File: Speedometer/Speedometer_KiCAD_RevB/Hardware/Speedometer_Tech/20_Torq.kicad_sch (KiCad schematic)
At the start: 20 parts, among them U204 WS2812B-4020_2, U205 WS2812B-4020_2, U206 WS2812B-4020_2, U207 WS2812B-4020_2, U208 WS2812B-4020_2, U209 WS2812B-4020_2, U210 WS2812B-4020_2, U211 WS2812B-4020_2, U212 WS2812B-4020_2, U213 WS2812B-4020_2, U214 WS2812B-4020_2, U215 WS2812B-4020_2, U216 WS2812B-4020_2, U217 WS2812B-4020_2, U218 WS2812B-4020_2, U219 WS2812B-4020_2, U220 WS2812B-4020_2, U221 WS2812B-4020_2, U222 WS2812B-4020_2, U223 WS2812B-4020_2

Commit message: updated troq display with new neopixel
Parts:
- added U224, U225, U226, U227, U228, U229, U230, U231, U232, U233, U234, U235, U236, U237, U238, U239, U240, U241: WS2812B-4020_2, LED_SMD:LED_WS2812B-2020_PLCC4_2.0x2.0mm, symbol LED:WS2812B-2020
- U204, U205, U206, U207, U208, U209, U210, U211: footprint LED_WS2812B-4020 -> LED_SMD:LED_WS2812B-2020_PLCC4_2.0x2.0mm; symbol Speedometer_Tech-altium-import:Designator_0_WS2812B-4020_2 -> LED:WS2812B-2020
- U212, U213, U214, U215, U216, U217, U218, U219, U220, U221, U222, U223: footprint LED_WS2812B-4020 -> LED_SMD:LED_WS2812B-2020_PLCC4_2.0x2.0mm; symbol Speedometer_Tech-altium-import:Designator_3_WS2812B-4020_2 -> LED:WS2812B-2020
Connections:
- net 5V: now also U204.4 (VDD), U205.4 (VDD), U206.4 (VDD), U207.4 (VDD), U208.4 (VDD), U209.4 (VDD), U210.4 (VDD), U211.4 (VDD), U212.4 (VDD), U213.4 (VDD), U214.4 (VDD), U215.4 (VDD), U216.4 (VDD), U217.4 (VDD), U218.4 (VDD), U219.4 (VDD), U220.4 (VDD), U221.4 (VDD), U222.4 (VDD), U223.4 (VDD), U224.4 (VDD), U225.4 (VDD), U226.4 (VDD), U227.4 (VDD), U228.4 (VDD), U229.4 (VDD), U230.4 (VDD), U231.4 (VDD), U232.4 (VDD), U233.4 (VDD), U234.4 (VDD), U235.4 (VDD), U236.4 (VDD), U237.4 (VDD), U238.4 (VDD), U239.4 (VDD), U240.4 (VDD), U241.4 (VDD); no longer U204.2 (VDD), U205.2 (VDD), U206.2 (VDD), U207.2 (VDD), U208.2 (VDD), U209.2 (VDD), U210.2 (VDD), U211.2 (VDD), U212.2 (VDD), U213.2 (VDD), U214.2 (VDD), U215.2 (VDD), U216.2 (VDD), U217.2 (VDD), U218.2 (VDD), U219.2 (VDD), U220.2 (VDD), U221.2 (VDD), U222.2 (VDD), U223.2 (VDD)
- net GND: now also U204.2 (VSS), U205.2 (VSS), U206.2 (VSS), U207.2 (VSS), U208.2 (VSS), U209.2 (VSS), U210.2 (VSS), U211.2 (VSS), U212.2 (VSS), U213.2 (VSS), U214.2 (VSS), U215.2 (VSS), U216.2 (VSS), U217.2 (VSS), U218.2 (VSS), U219.2 (VSS), U220.2 (VSS), U221.2 (VSS), U222.2 (VSS), U223.2 (VSS), U224.2 (VSS), U225.2 (VSS), U226.2 (VSS), U227.2 (VSS), U228.2 (VSS), U229.2 (VSS), U230.2 (VSS), U231.2 (VSS), U232.2 (VSS), U233.2 (VSS), U234.2 (VSS), U235.2 (VSS), U236.2 (VSS), U237.2 (VSS), U238.2 (VSS), U239.2 (VSS), U240.2 (VSS), U241.2 (VSS); no longer U204.4 (VSS), U205.4 (VSS), U206.4 (VSS), U207.4 (VSS), U208.4 (VSS), U209.4 (VSS), U210.4 (VSS), U211.4 (VSS), U212.4 (VSS), U213.4 (VSS), U214.4 (VSS), U215.4 (VSS), U216.4 (VSS), U217.4 (VSS), U218.4 (VSS), U219.4 (VSS), U220.4 (VSS), U221.4 (VSS), U222.4 (VSS), U223.4 (VSS)
- net TorqIn: now also U204.3 (DIN); no longer U204.1 (DIN)
- net TorqOut: now also U241.1 (DOUT); no longer U223.3 (DOUT)
- net at U219.1 (DOUT): now also U220.3 (DIN); no longer U218.3 (DOUT)
- net at U219.3 (DIN): now also U218.1 (DOUT); no longer U220.1 (DIN)
- net at U211.1 (DOUT): now also U212.3 (DIN); no longer U210.3 (DOUT)
- net at U211.3 (DIN): now also U210.1 (DOUT); no longer U212.1 (DIN)
- net at U217.1 (DOUT): now also U218.3 (DIN); no longer U216.3 (DOUT)
- net at U217.3 (DIN): now also U216.1 (DOUT); no longer U218.1 (DIN)
- net at U215.1 (DOUT): now also U216.3 (DIN); no longer U214.3 (DOUT)
- net at U215.3 (DIN): now also U214.1 (DOUT); no longer U216.1 (DIN)
- net at U213.1 (DOUT): now also U214.3 (DIN); no longer U212.3 (DOUT)
- net at U213.3 (DIN): now also U212.1 (DOUT); no longer U214.1 (DIN)
- net at U205.1 (DOUT): now also U206.3 (DIN); no longer U204.3 (DOUT)
- net at U205.3 (DIN): now also U204.1 (DOUT); no longer U206.1 (DIN)
- net at U223.1 (DOUT): now also U224.3 (DIN); no longer U222.3 (DOUT)
- net at U209.1 (DOUT): now also U210.3 (DIN); no longer U208.3 (DOUT)
- net at U209.3 (DIN): now also U208.1 (DOUT); no longer U210.1 (DIN)
- net at U221.1 (DOUT): now also U222.3 (DIN); no longer U220.3 (DOUT)
- net at U222.1 (DOUT): now also U223.3 (DIN); no longer U221.3 (DOUT)
- net at U207.3 (DIN): now also U206.1 (DOUT); no longer U208.1 (DIN)
- net at U207.1 (DOUT): now also U208.3 (DIN); no longer U206.3 (DOUT)
- new net: U224.1 (DOUT), U225.3 (DIN)
- new net: U225.1 (DOUT), U226.3 (DIN)
- new net: U231.1 (DOUT), U232.3 (DIN)
- new net: U230.1 (DOUT), U231.3 (DIN)
- new net: U236.1 (DOUT), U237.3 (DIN)
- new net: U235.1 (DOUT), U236.3 (DIN)
- new net: U229.1 (DOUT), U230.3 (DIN)
- new net: U228.1 (DOUT), U229.3 (DIN)
- new net: U238.1 (DOUT), U239.3 (DIN)
- new net: U237.1 (DOUT), U238.3 (DIN)
- new net: U234.1 (DOUT), U235.3 (DIN)
- new net: U233.1 (DOUT), U234.3 (DIN)
- new net: U220.1 (DOUT), U221.3 (DIN)
- new net: U227.1 (DOUT), U228.3 (DIN)
- new net: U226.1 (DOUT), U227.3 (DIN)
- new net: U240.1 (DOUT), U241.3 (DIN)
- new net: U239.1 (DOUT), U240.3 (DIN)
- new net: U232.1 (DOUT), U233.3 (DIN)

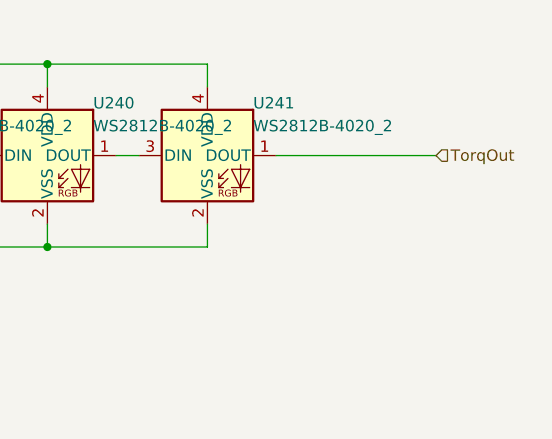
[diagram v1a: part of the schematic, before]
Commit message: current version of lada speedometer in kicad
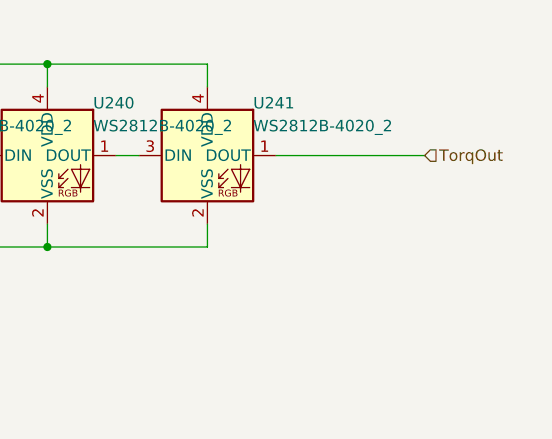
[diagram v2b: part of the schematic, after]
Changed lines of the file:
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@@
-	(wire
-		(pts
-			(xy 417.83 -17.78) (xy 435.61 -17.78)
-		)
-		(stroke
-			(width 0)
-			(type default)
-		)
-	)
 	(wire
 		(pts
@@
 		(pts
 			(xy 49.53 279.4) (xy 52.07 279.4)
+		)
+		(stroke
+			(width 0)
+			(type default)
+		)
+	)
+	(wire
+		(pts
+			(xy 434.34 -17.78) (xy 417.83 -17.78)
 		)
 		(stroke
@@
 	(hierarchical_label "TorqOut"
 		(shape input)
-		(at 435.61 -17.78 0)
+		(at 434.34 -17.78 0)
 		(effects
 			(font

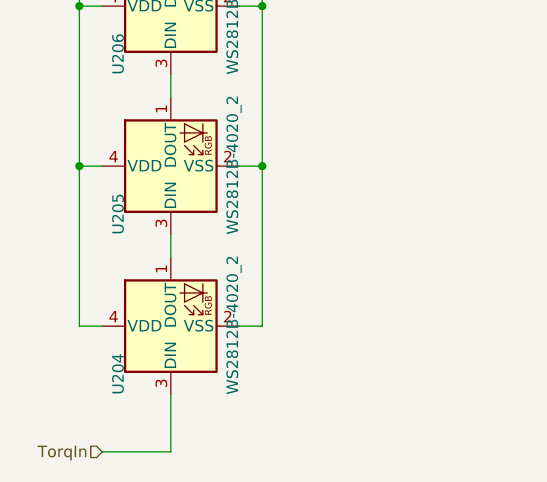
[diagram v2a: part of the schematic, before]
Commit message: Speedometer DRC mostly passed
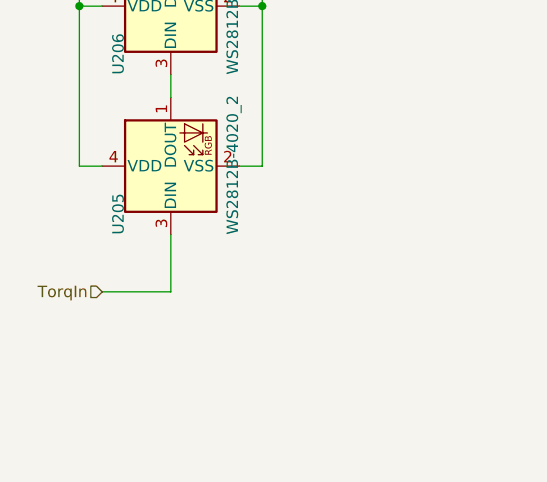
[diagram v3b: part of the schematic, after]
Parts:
- removed U204: WS2812B-4020_2, LED_SMD:LED_WS2812B-2020_PLCC4_2.0x2.0mm, symbol LED:WS2812B-2020
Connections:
- net TorqIn: now also U205.3 (DIN)
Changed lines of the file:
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@@
 	)
 	(junction
-		(at 52.07 261.62)
-		(diameter 0)
-		(color 0 0 0 0)
-	)
-	(junction
 		(at 267.97 -27.94)
 		(diameter 0)
@@
 	)
 	(junction
-		(at 31.75 261.62)
-		(diameter 0)
-		(color 0 0 0 0)
-	)
-	(junction
 		(at 52.07 -5.08)
 		(diameter 0)
@@
 	(wire
 		(pts
-			(xy 31.75 279.4) (xy 34.29 279.4)
-		)
-		(stroke
-			(width 0)
-			(type default)
-		)
-	)
-	(wire
-		(pts
 			(xy 346.71 -17.78) (xy 349.25 -17.78)
 		)
@@
 	(wire
 		(pts
-			(xy 52.07 261.62) (xy 52.07 279.4)
-		)
-		(stroke
-			(width 0)
-			(type default)
-		)
-	)
-	(wire
-		(pts
 			(xy 285.75 -27.94) (xy 285.75 -25.4)
 		)
@@
 	(wire
 		(pts
-			(xy 41.91 269.24) (xy 41.91 271.78)
-		)
-		(stroke
-			(width 0)
-			(type default)
-		)
-	)
-	(wire
-		(pts
 			(xy 49.53 226.06) (xy 52.07 226.06)
 		)
@@
 	(wire
 		(pts
-			(xy 31.75 261.62) (xy 31.75 279.4)
-		)
-		(stroke
-			(width 0)
-			(type default)
-		)
-	)
-	(wire
-		(pts
 			(xy 52.07 172.72) (xy 52.07 190.5)
 		)
@@
 	(wire
 		(pts
-			(xy 34.29 293.37) (xy 41.91 293.37)
+			(xy 34.29 275.59) (xy 41.91 275.59)
 		)
 		(stroke
@@
 	(wire
 		(pts
-			(xy 41.91 287.02) (xy 41.91 293.37)
+			(xy 41.91 269.24) (xy 41.91 275.59)
 		)
 		(stroke
@@
 	(wire
 		(pts
-			(xy 49.53 279.4) (xy 52.07 279.4)
-		)
-		(stroke
-			(width 0)
-			(type default)
-		)
-	)
-	(wire
-		(pts
 			(xy 434.34 -17.78) (xy 417.83 -17.78)
 		)
@@
 	(hierarchical_label "TorqIn"
 		(shape input)
-		(at 34.29 293.37 180)
+		(at 34.29 275.59 180)
 		(effects
 			(font
@@
 			)
 		)
-		(property "Description" ""
+		(property "Description" "Power symbol creates a global label with name 'GND'"
 			(at 90.17 -7.62 0)
 			(effects
@@
 	(symbol
 		(lib_id "LED:WS2812B-2020")
-		(at 41.91 279.4 90)
-		(unit 1)
-		(exclude_from_sim no)
-		(in_bom yes)
-		(on_board yes)
-		(dnp no)
-		(property "Reference" "U204"
-			(at 36.83 287.02 0)
-			(effects
-				(font
-					(size 1.27 1.27)
-				)
-				(justify left bottom)
-			)
-		)
-		(property "Value" "WS2812B-4020_2"
-			(at 49.53 287.02 0)
-			(effects
-				(font
-					(size 1.27 1.27)
-				)
-				(justify left bottom)
-			)
-		)
-		(property "Footprint" "LED_SMD:LED_WS2812B-2020_PLCC4_2.0x2.0mm"
-			(at 49.53 278.13 0)
-			(effects
-				(font
-					(size 1.27 1.27)
-				)
-				(justify left top)
-				(hide yes)
-			)
-		)
-		(property "Datasheet" "https://cdn-shop.adafruit.com/product-files/4684/4684_WS2812B-2020_V1.3_EN.pdf"
-			(at 51.435 276.86 0)
-			(effects
-				(font
-					(size 1.27 1.27)
-				)
-				(justify left top)
-				(hide yes)
-			)
-		)
-		(property "Description" "RGB LED with integrated controller, 2.0 x 2.0 mm, 12 mA"
-			(at 41.91 279.4 0)
-			(effects
-				(font
-					(size 1.27 1.27)
-				)
-				(hide yes)
-			)
-		)
-		(property "PRICE" "None"
-			(at 36.83 292.608 0)
-			(effects
-				(font
-					(size 1.27 1.27)
-				)
-				(justify left bottom)
-				(hide yes)
-			)
-		)
-		(property "MP" "WS2812B-4020"
-			(at 36.83 292.608 0)
-			(effects
-				(font
-					(size 1.27 1.27)
-				)
-				(justify left bottom)
-				(hide yes)
-			)
-		)
-		(property "AVAILABILITY" "Not in stock"
-			(at 36.83 292.608 0)
-			(effects
-				(font
-					(size 1.27 1.27)
-				)
-				(justify left bottom)
-				(hide yes)
-			)
-		)
-		(property "SNAPEDA_LINK" "https://www.snapeda.com/parts/WS2812B-4020/Worldsemi/view-part/?ref=snap"
-			(at 36.83 292.608 0)
-			(effects
-				(font
-					(size 1.27 1.27)
-				)
-				(justify left bottom)
-				(hide yes)
-			)
-		)
-		(property "CHECK_PRICES" "https://www.snapeda.com/parts/WS2812B-4020/Worldsemi/view-part/?ref=eda"
-			(at 36.83 292.608 0)
-			(effects
-				(font
-					(size 1.27 1.27)
-				)
-				(justify left bottom)
-				(hide yes)
-			)
-		)
-		(property "ALTIUM_VALUE" "*"
-			(at 36.83 292.608 0)
-			(effects
-				(font
-					(size 1.27 1.27)
-				)
-				(justify left bottom)
-				(hide yes)
-			)
-		)
-		(property "PACKAGE" "Package"
-			(at 36.83 292.608 0)
-			(effects
-				(font
-					(size 1.27 1.27)
-				)
-				(justify left bottom)
-				(hide yes)
-			)
-		)
-		(property "MF" "Worldsemi"
-			(at 36.83 292.608 0)
-			(effects
-				(font
-					(size 1.27 1.27)
-				)
-				(justify left bottom)
-				(hide yes)
-			)
-		)
-		(pin "1"
-		)
-		(pin "2"
-		)
-		(pin "3"
-		)
-		(pin "4"
-		)
-		(instances
-			(project ""
-				(path "/7a911dfa-7957-409a-ad31-10c26a0bf949/de88d757-f807-4a53-8f0b-a2d0f7ee584a"
-					(reference "U204")
-					(unit 1)
-				)
-			)
-		)
-	)
-	(symbol
-		(lib_id "LED:WS2812B-2020")
 		(at 72.39 -17.78 0)
 		(unit 1)
@@
 			)
 		)
-		(property "Description" ""
+		(property "Description" "Power symbol creates a global label with name '5V'"
 			(at 90.17 -27.94 0)
 			(effects
